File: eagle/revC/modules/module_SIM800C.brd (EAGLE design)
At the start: 24.1 x 32.8 mm, 11 parts, among them IC1 SIM800C, X1 734120110

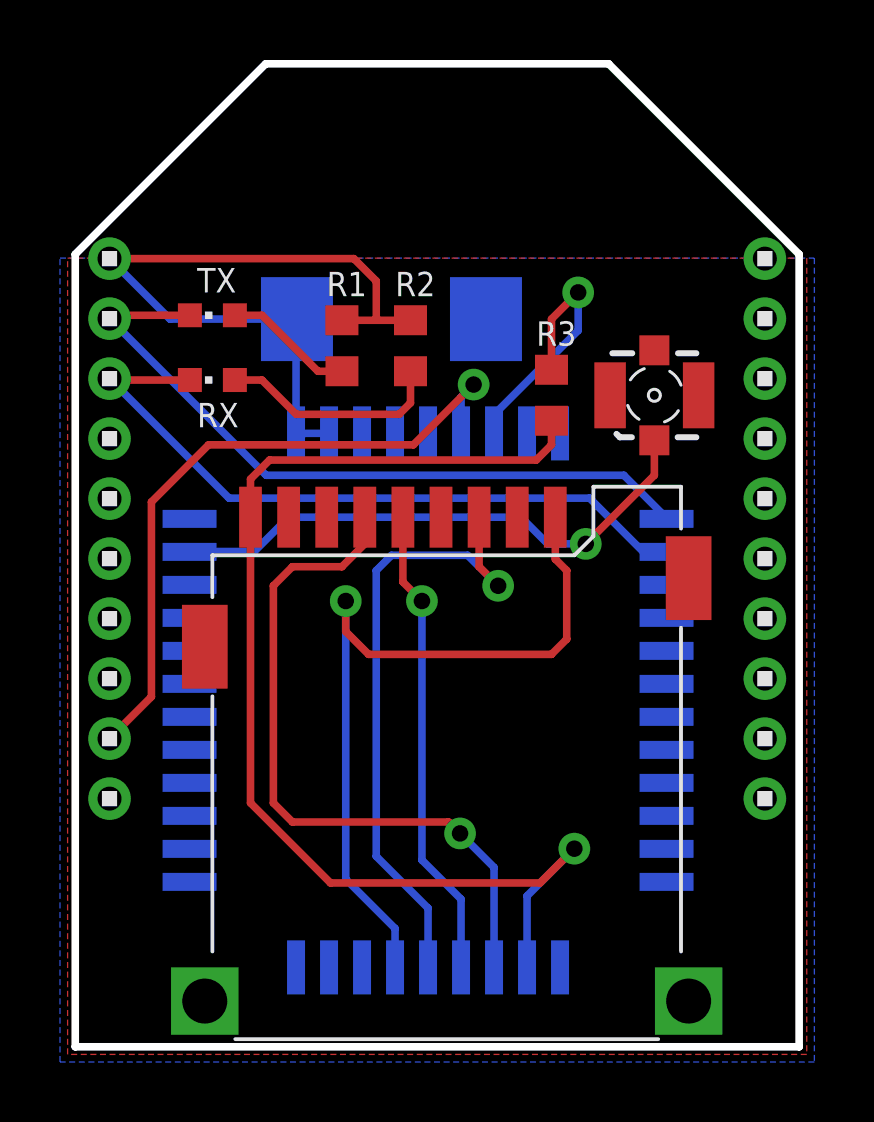
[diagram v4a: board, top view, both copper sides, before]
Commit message: Fixed module name layers
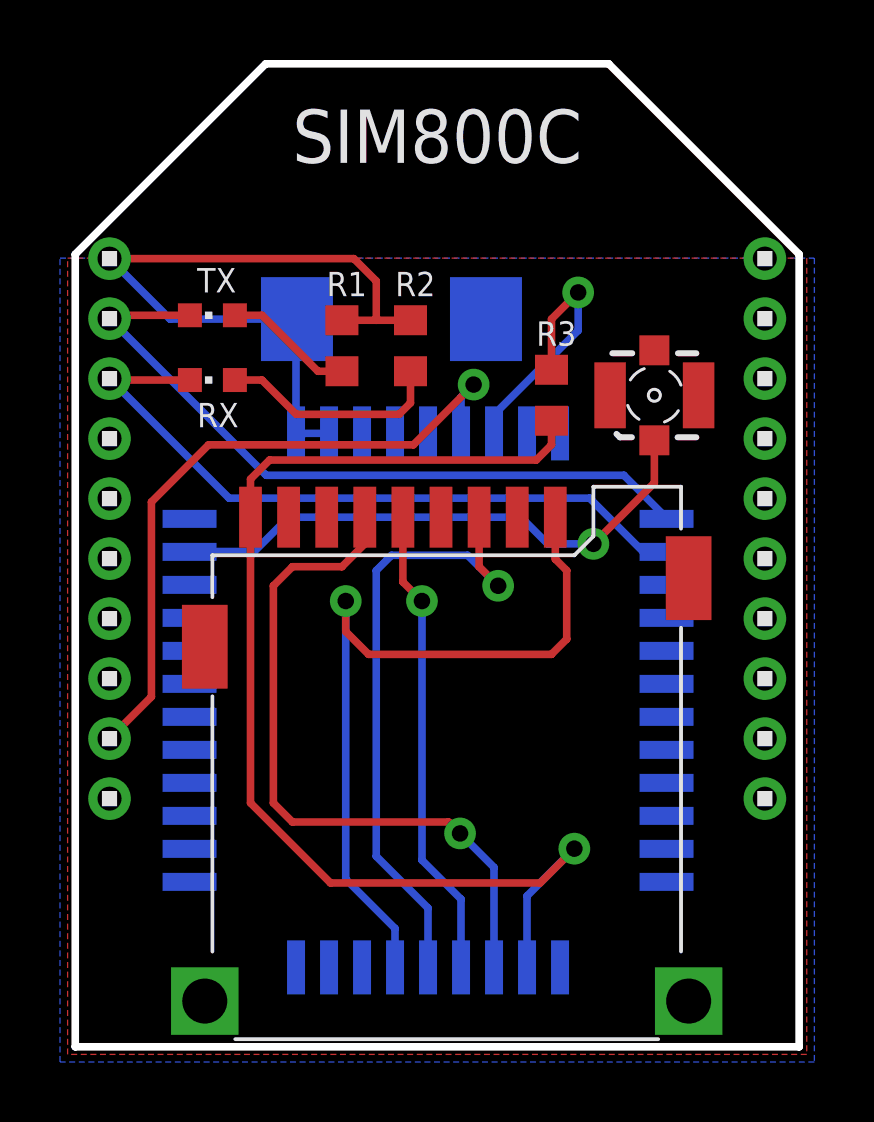
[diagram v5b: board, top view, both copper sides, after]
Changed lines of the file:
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@@
 <wire x1="24.257" y1="26.543" x2="24.257" y2="0.127" width="0.254" layer="20"/>
 <wire x1="24.257" y1="0.127" x2="0.127" y2="0.127" width="0.254" layer="20"/>
-<text x="12.192" y="30.48" size="1.778" layer="51" ratio="15" rot="SR0" align="center">SIM800C</text>
-<text x="5.461" y="25.4" size="0.8128" layer="52" font="vector" ratio="12" rot="SR0" align="center">+</text>
+<text x="12.192" y="30.48" size="1.778" layer="25" ratio="15" rot="SR0" align="center">SIM800C</text>
+<text x="5.461" y="25.4" size="0.8128" layer="26" font="vector" ratio="12" rot="SR0" align="center">+</text>
 <text x="5.842" y="21.971" size="0.8128" layer="126" font="vector" ratio="12" rot="SMR0">C1</text>
 <text x="8.509" y="25.146" size="0.8128" layer="125" font="vector" ratio="12" rot="SR0">R1</text>
@@
 <element name="RIGHT1" library="headers(2mm)" package="1X10" value="1X10" x="23.114" y="17.399" smashed="yes" rot="R270"/>
 <element name="X1" library="con-coax" library_urn="urn:adsk.eagle:library:133" package="734120110" package3d_urn="urn:adsk.eagle:package:6199/1" value="734120110" x="19.431" y="21.844" smashed="yes"/>
-<element name="IC1" library="RadioShield" package="SIM800C" value="SIM800C" x="11.887" y="11.674" smashed="yes" rot="MR0">
-<attribute name="VALUE" x="12.120659375" y="11.722640625" size="0.8128" layer="52" font="vector" ratio="12" rot="SMR0" align="center"/>
-</element>
+<element name="IC1" library="RadioShield" package="SIM800C" value="SIM800C" x="11.887" y="11.674" smashed="yes" rot="MR0"/>
 <element name="R1" library="rcl" library_urn="urn:adsk.eagle:library:334" package="R0603" package3d_urn="urn:adsk.eagle:package:23555/3" value="1k" x="9.017" y="23.495" smashed="yes" rot="R90">
 <attribute name="NAME" x="8.509" y="25.146" size="0.8128" layer="25" font="vector" ratio="12" rot="SR0"/>
@@
 <contactref element="X1" pad="1"/>
 <wire x1="3.95" y1="16.637" x2="3.937" y2="16.624" width="0.254" layer="16"/>
-<wire x1="19.431" y1="19.177" x2="19.431" y2="20.344" width="0.254" layer="1"/>
-<via x="17.145" y="16.891" extent="1-16" drill="0.55"/>
-<wire x1="17.145" y1="16.891" x2="19.431" y2="19.177" width="0.254" layer="1"/>
+<via x="17.399" y="16.891" extent="1-16" drill="0.55"/>
 <wire x1="6.096" y1="16.637" x2="3.95" y2="16.637" width="0.254" layer="16"/>
-<wire x1="17.145" y1="16.891" x2="15.875" y2="16.891" width="0.254" layer="16"/>
+<wire x1="17.399" y1="16.891" x2="15.875" y2="16.891" width="0.254" layer="16"/>
 <wire x1="15.875" y1="16.891" x2="14.986" y2="17.78" width="0.254" layer="16"/>
 <wire x1="14.986" y1="17.78" x2="7.239" y2="17.78" width="0.254" layer="16"/>
 <wire x1="7.239" y1="17.78" x2="6.096" y2="16.637" width="0.254" layer="16"/>
+<wire x1="19.431" y1="18.923" x2="19.431" y2="20.344" width="0.254" layer="1"/>
+<wire x1="17.399" y1="16.891" x2="19.431" y2="18.923" width="0.254" layer="1"/>
 </signal>
 <signal name="UART_TX">
